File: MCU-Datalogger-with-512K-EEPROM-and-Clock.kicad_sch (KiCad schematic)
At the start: 0 parts

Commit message: updated git ignore
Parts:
- added BT1: Battery, symbol Device:Battery
- added C1, C2, C3, C4: C, symbol Device:C
- added C5: C_Polarized, symbol Device:C_Polarized
- added D1, D2: LED, symbol Device:LED
- added R1, R2, R3, R4, R5, R6, R7: R, symbol Device:R
- added U1, U2: 24LC1025, symbol Memory_EEPROM:24LC1025
- added U3: ATMEGA328P-AU, ATMEGA328P-AU:QFP80P900X900X120-32N, symbol ATMEGA328P-AU:ATMEGA328P-AU
- added U4: DS1337S_, DS1337S_:SOIC127P600X175-8N, symbol DS1337S_:DS1337S_
- added Y1, Y2: Crystal, symbol Device:Crystal
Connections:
- new net: BT1.1 (+), C5.1, D2.2 (A), U3.18 (AVCC), U3.4 (VCC)
- new net: C4.1, U3.20 (AREF)
- new net: C2.2, U3.7 (PB6), Y2.1
- new net: C3.1, U3.8 (PB7), Y2.2
- new net: D1.1 (K), R5.2
- new net: U4.2 (X2), Y1.1
- new net: U4.1 (X1), Y1.2
- new net: R1.2, U4.3 (~{INTA})
- new net: R2.2, U4.7 (SQW/~INT)
- new net: D2.1 (K), R7.1
- new net D2: U3.32 (PD2)
- new net D3: U3.1 (PD3)
- new net D4: U3.2 (PD4)
- new net D5: U3.9 (PD5)
- new net D6: U3.10 (PD6)
- new net D7: U3.11 (PD7)
- new net DB: U3.12 (PB0)
- new net GND: BT1.2 (-), C1.2, C2.1, C3.2, C4.2, C5.2, R5.1, R7.2, U1.4 (GND), U1.7 (WP), U2.2 (A1), U2.4 (GND), U2.7 (WP), U3.21 (GND), U3.3 (GND), U3.5 (GND), U4.4 (GND)
- new net MISO: U3.16 (PB4)
- new net MOSI: U3.15 (PB3)
- new net RESET: R6.1, U3.29 (PC6/~{RESET})
- new net RX: U3.30 (PD0)
- new net SCL: D1.2 (A), R3.2, U1.6 (SCL), U2.6 (SCL), U3.17 (PB5), U3.28 (PC5), U4.6 (SCL)
- new net SDA: R4.2, U1.5 (SDA), U2.5 (SDA), U3.27 (PC4), U4.5 (SDA)
- new net TX: U3.31 (PD1)
- new net Vcc: C1.1, R1.1, R2.1, R3.1, R4.1, R6.2, U1.1 (A0), U1.2 (A1), U1.3 (A2), U1.8 (VCC), U2.1 (A0), U2.3 (A2), U2.8 (VCC), U4.8 (VCC)
- no-connect marks 0 -> 9

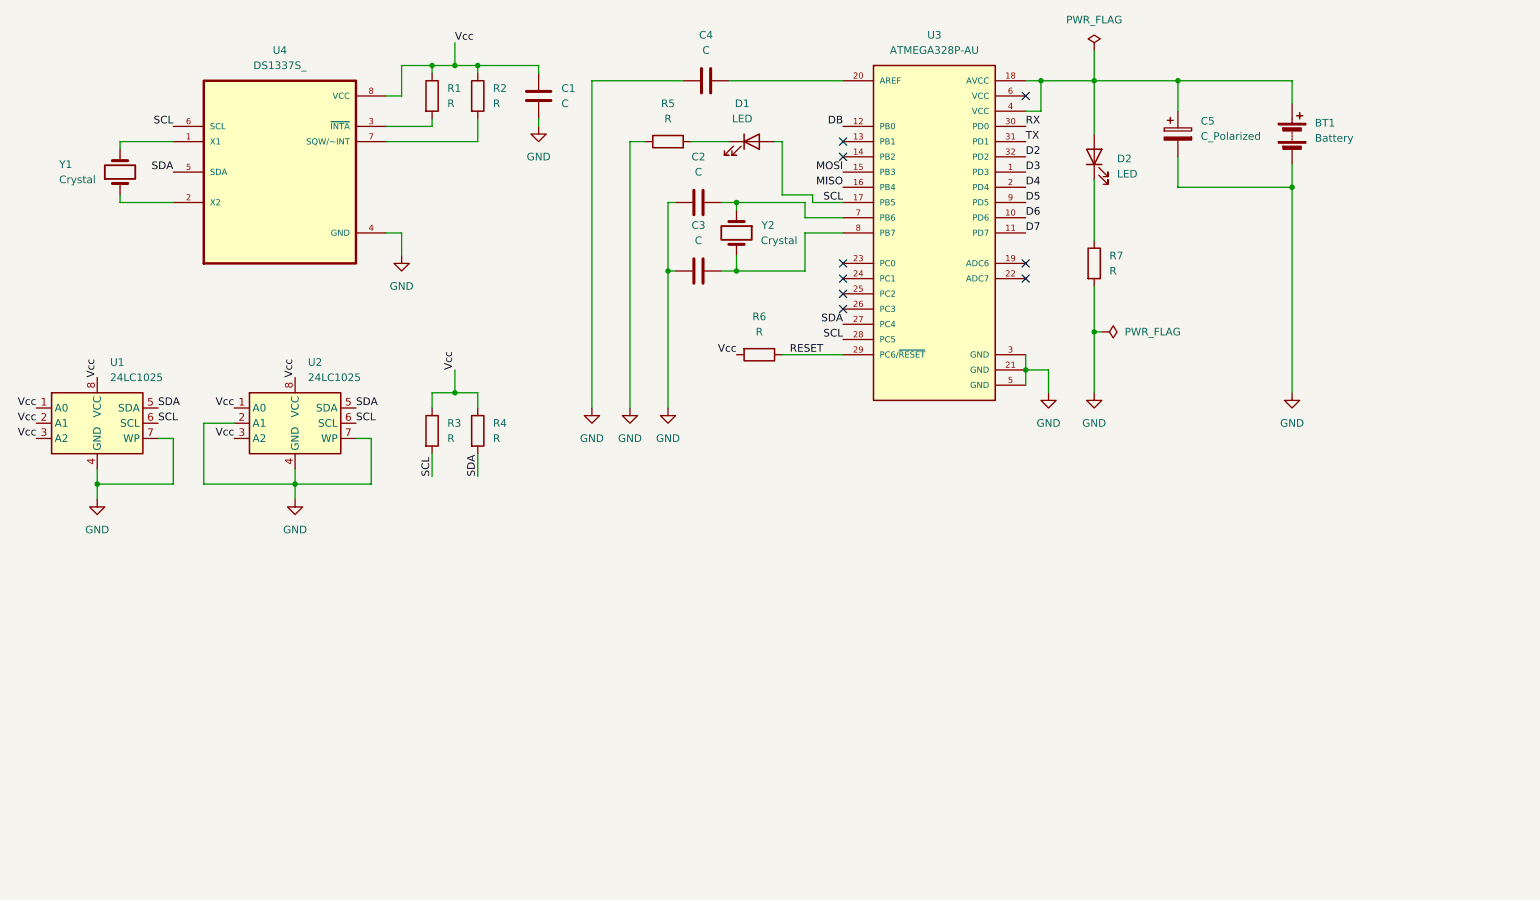
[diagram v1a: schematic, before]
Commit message: finalized schematic
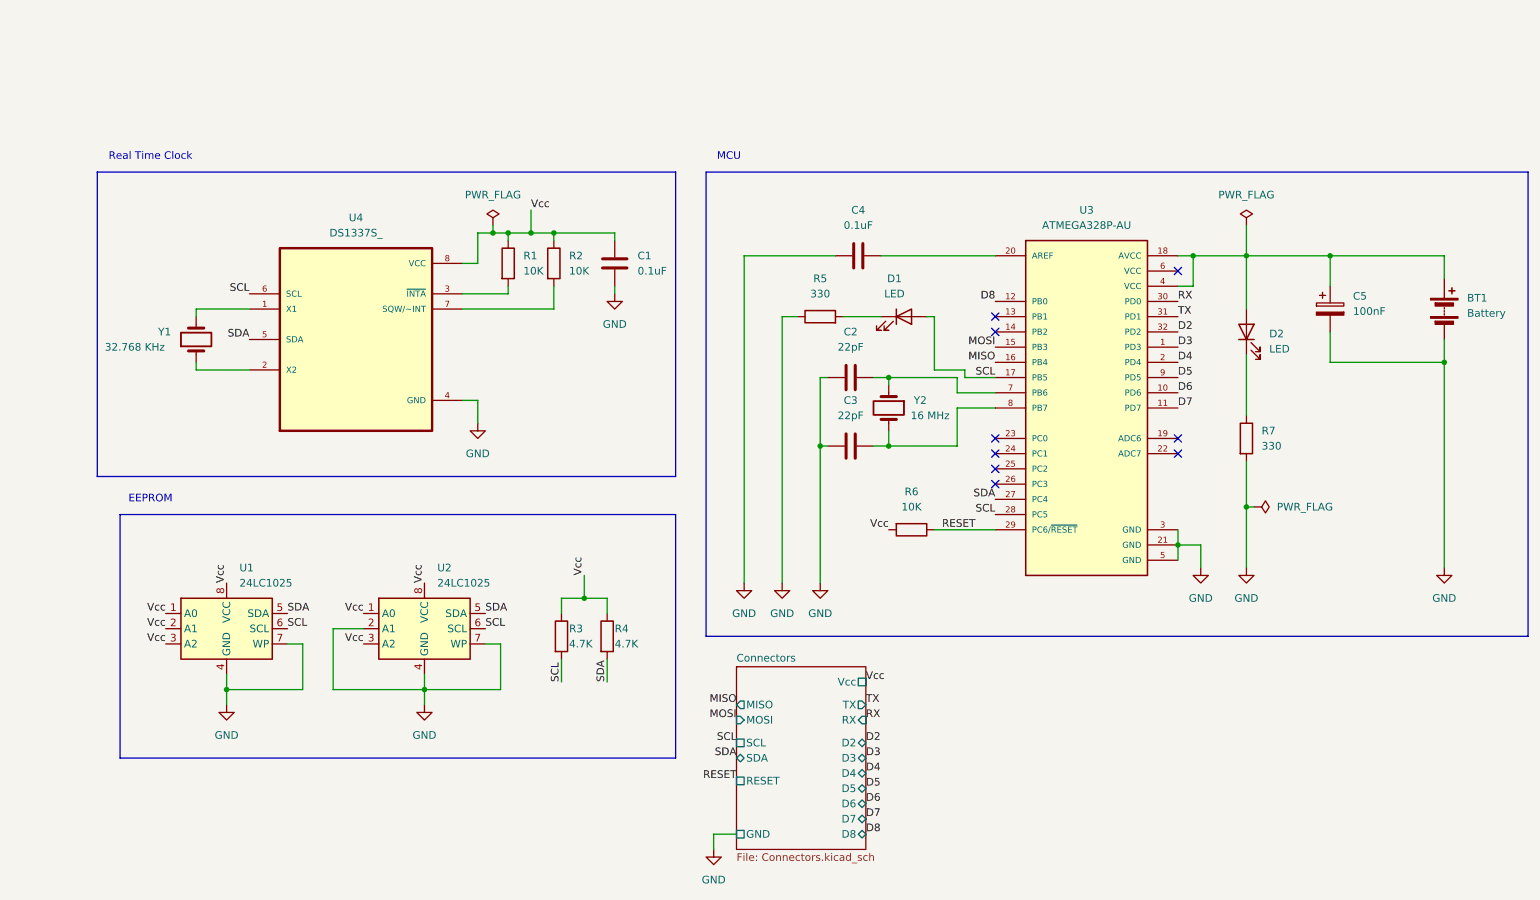
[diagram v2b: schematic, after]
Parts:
- BT1: footprint (none) -> Connector_PinHeader_2.54mm:PinHeader_1x02_P2.54mm_Vertical
- C1, C4: value C -> 0.1uF; footprint (none) -> Capacitor_SMD:C_0805_2012Metric
- C2, C3: value C -> 22pF; footprint (none) -> Capacitor_SMD:C_0805_2012Metric
- C5: value C_Polarized -> 100nF; footprint (none) -> Capacitor_SMD:C_0805_2012Metric
- D1, D2: footprint (none) -> LED_SMD:LED_0805_2012Metric
- R1, R2, R6: value R -> 10K; footprint (none) -> Resistor_SMD:R_0805_2012Metric
- R3, R4: value R -> 4.7K; footprint (none) -> Resistor_SMD:R_0805_2012Metric
- R5, R7: value R -> 330; footprint (none) -> Resistor_SMD:R_0805_2012Metric
- U1, U2: footprint (none) -> Package_SO:SOIC-8_5.3x5.3mm_P1.27mm
- Y1: value Crystal -> 32.768 KHz; footprint (none) -> Crystal:Crystal_SMD_5032-2Pin_5.0x3.2mm_HandSoldering
- Y2: value Crystal -> 16 MHz; footprint (none) -> Crystal:Crystal_SMD_5032-2Pin_5.0x3.2mm_HandSoldering
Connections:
- net DB renamed D8
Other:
- added sheet Connectors (Connectors.kicad_sch)
- note added: "EEPROM"
- note added: "MCU"
- note added: "Real Time Clock"
- moved on the sheet: BT1, C1, C2, C3, C4, C5, D1, D2, R1, R2, R3, R4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

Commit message: uploaded page setting; restarting the board design
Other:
- company: University of Notre Dame | Udemy -> ${company_name}
- title: MCU Datalogger with 512K EEPROM and Clock -> ${project_name}
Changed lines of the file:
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@@
 	(paper "A4")
 	(title_block
-		(title "MCU Datalogger with 512K EEPROM and Clock")
+		(title "${project_name}")
 		(date "2025-07-04")
 		(rev "1")
-		(company "University of Notre Dame | Udemy")
-		(comment 1 "Made by Andres Perez")
+		(company "${company_name}")
+		(comment 1 "${comment_1}")
 	)
 	(rectangle

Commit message: 2 layer board completed; minus annotation and further design rule checking
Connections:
- net Vcc: now also BT1.1 (+), C5.1, D2.2 (A), U3.18 (AVCC), U3.4 (VCC)
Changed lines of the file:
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@@
+		)
+	)
+	(label "Vcc"
+		(at 227.33 55.88 180)
+		(effects
+			(font
+				(size 1.27 1.27)
+			)
+			(justify right bottom)
 		)
 	)

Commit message: fixed schematic sck vs scl nets
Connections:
- net SCL: no longer D1.2 (A), U3.17 (PB5)
- new net SCK: D1.2 (A), U3.17 (PB5)
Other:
- sheet Connectors ports: added SCK; removed none
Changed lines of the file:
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@@
 	(wire
 		(pts
-			(xy 220.98 50.8) (xy 220.98 55.88)
-		)
-		(stroke
-			(width 0)
-			(type default)
-		)
-	)
-	(wire
-		(pts
 			(xy 160.02 55.88) (xy 179.07 55.88)
 		)
@@
 		)
 	)
+	(label "SCK"
+		(at 135.89 146.05 180)
+		(effects
+			(font
+				(size 1.27 1.27)
+			)
+			(justify right bottom)
+		)
+	)
 	(label "SDA"
 		(at 93.98 115.57 0)
@@
 		)
 	)
-	(label "SCL"
+	(label "SCK"
 		(at 179.07 76.2 180)
 		(effects
@@
 	)
 	(symbol
-		(lib_id "power:PWR_FLAG")
-		(at 220.98 50.8 0)
-		(unit 1)
-		(exclude_from_sim no)
-		(in_bom yes)
-		(on_board yes)
-		(dnp no)
-		(fields_autoplaced yes)
-		(property "Reference" "#FLG01"
-			(at 220.98 48.895 0)
-			(effects
-				(font
-					(size 1.27 1.27)
-				)
-				(hide yes)
-			)
-		)
-		(property "Value" "PWR_FLAG"
-			(at 220.98 45.72 0)
-			(effects
-				(font
-					(size 1.27 1.27)
-				)
-			)
-		)
-		(property "Footprint" ""
-			(at 220.98 50.8 0)
-			(effects
-				(font
-					(size 1.27 1.27)
-				)
-				(hide yes)
-			)
-		)
-		(property "Datasheet" "~"
-			(at 220.98 50.8 0)
-			(effects
-				(font
-					(size 1.27 1.27)
-				)
-				(hide yes)
-			)
-		)
-		(property "Description" "Special symbol for telling ERC where power comes from"
-			(at 220.98 50.8 0)
-			(effects
-				(font
-					(size 1.27 1.27)
-				)
-				(hide yes)
-			)
-		)
-		(pin "1"
-		)
-		(instances
-			(project ""
-				(path "/776834cb-092e-4fc8-9e79-814f53597284"
-					(reference "#FLG01")
-					(unit 1)
-				)
-			)
-		)
-	)
-	(symbol
 		(lib_id "Device:R")
 		(at 149.86 66.04 90)
@@
 			(effects
 				(font
+					(size 1.27 1.27)
+				)
+				(justify left)
+			)
+		)
+		(pin "SCK" passive
+			(at 135.89 146.05 180)
+			(effects
+				(font
